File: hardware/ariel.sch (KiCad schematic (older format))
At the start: 18 parts, among them SW1 SW_Push, U1 74HC595, U2 Si7020-A20, U3 WeMos_D1_mini

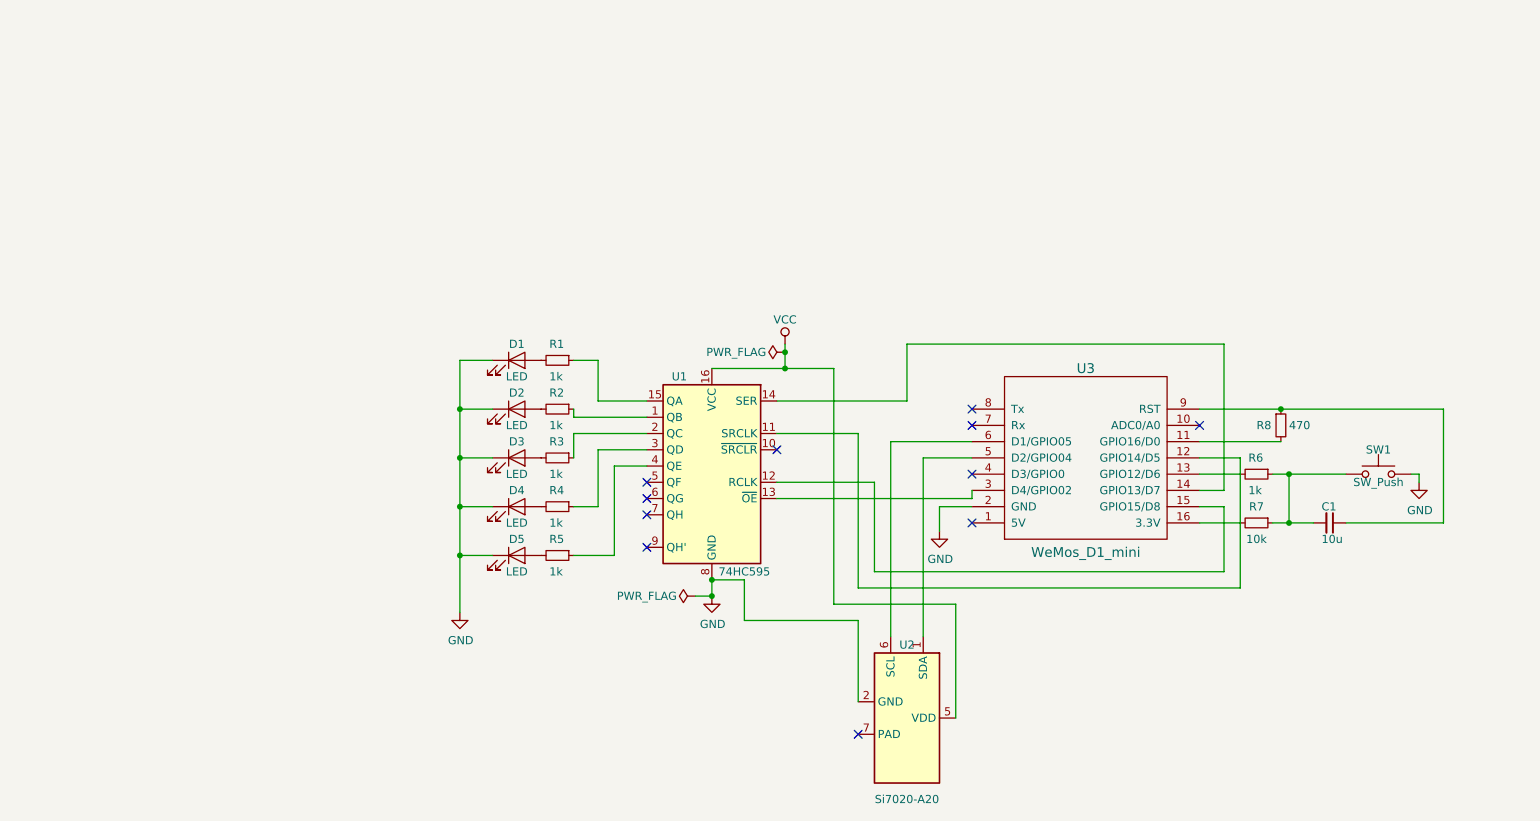
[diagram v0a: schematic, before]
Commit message: Fix power input and output
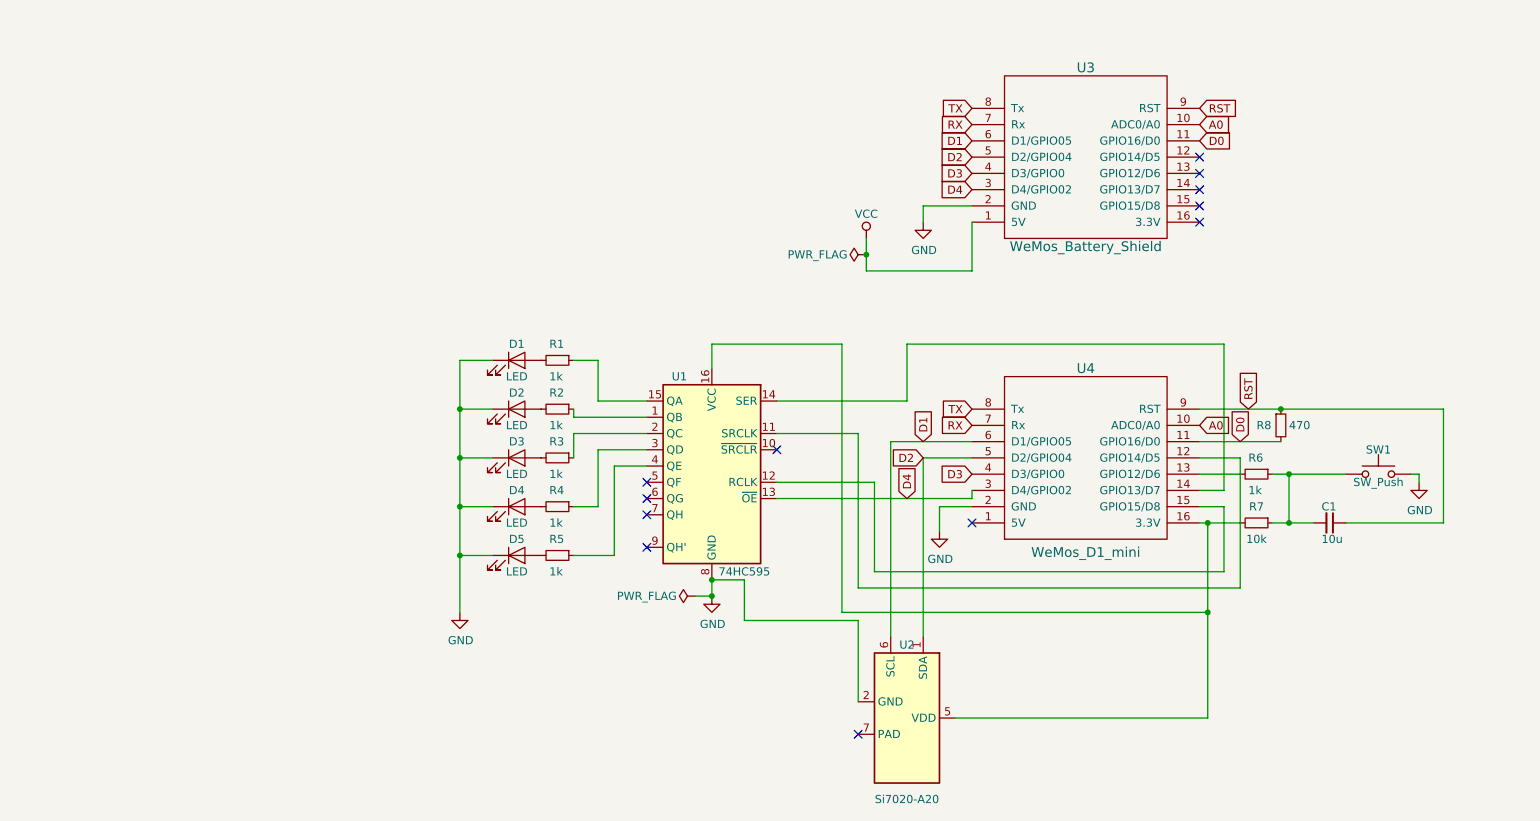
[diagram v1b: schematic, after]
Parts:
- added U3: WeMos_Battery_Shield, symbol wemos_mini:WeMos_Battery_Shield
- renumbered U3 to U4
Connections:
- net GND: now also U3.2 (GND)
- net VCC: now also U3.1 (5V); no longer U1.16 (VCC), U2.5 (VDD)
- net D4: now reaches U1.13 (~OE), U4.3 (D4/GPIO02)
- net D4: now also U3.3 (D4/GPIO02)
- net A0: now reaches U4.10 (ADC0/A0)
- net A0: now also U3.10 (ADC0/A0)
- net D0: now reaches R8.2, U4.11 (GPIO16/D0)
- net D0: now also U3.11 (GPIO16/D0)
- net at R7.2, U4.16 (3.3V): now also U1.16 (VCC), U2.5 (VDD)
- net D3: now reaches U4.4 (D3/GPIO0)
- net D3: now also U3.4 (D3/GPIO0)
- net D2: now reaches U2.1 (SDA), U4.5 (D2/GPIO04)
- net D2: now also U3.5 (D2/GPIO04)
- net D1: now reaches U2.6 (SCL), U4.6 (D1/GPIO05)
- net D1: now also U3.6 (D1/GPIO05)
- net RX: now reaches U4.7 (Rx)
- net RX: now also U3.7 (Rx)
- net TX: now reaches U4.8 (Tx)
- net TX: now also U3.8 (Tx)
- net RST: now reaches C1.1, R8.1, U4.9 (RST)
- net RST: now also U3.9 (RST)
- no-connect marks 11 -> 12
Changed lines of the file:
@@
 $EndComp
 $Comp
-L wemos_mini:WeMos_D1_mini U3
+L wemos_mini:WeMos_D1_mini U4
 U 1 1 5C77373A
 P 7500 3450
-F 0 "U3" H 7500 2900 60  0000 C CNN
+F 0 "U4" H 7500 2900 60  0000 C CNN
 F 1 "WeMos_D1_mini" H 7500 4031 60  0000 C CNN
 F 2 "" H 7900 2750 60  0000 C CNN
@@
 	8200 3350 8700 3350
 $Comp
-L power:GND #PWR04
+L power:GND #PWR06
 U 1 1 5C8607DD
 P 9550 3600
-F 0 "#PWR04" H 9550 3350 50  0001 C CNN
+F 0 "#PWR06" H 9550 3350 50  0001 C CNN
 F 1 "GND" H 9555 3427 50  0000 C CNN
 F 2 "" H 9550 3600 50  0001 C CNN
@@
 Connection ~ 8700 3150
 $Comp
-L power:GND #PWR03
+L power:GND #PWR05
 U 1 1 5C8612CC
 P 6600 3900
-F 0 "#PWR03" H 6600 3650 50  0001 C CNN
+F 0 "#PWR05" H 6600 3650 50  0001 C CNN
 F 1 "GND" H 6605 3727 50  0000 C CNN
 F 2 "" H 6600 3900 50  0001 C CNN
@@
 Wire Wire Line
 	8450 3450 8200 3450
-Wire Wire Line
-	5950 4350 5950 2900
-$Comp
-L power:PWR_FLAG #FLG01
+$Comp
+L power:PWR_FLAG #FLG02
 U 1 1 5C86A0B5
-P 5650 2800
-F 0 "#FLG01" H 5650 2875 50  0001 C CNN
-F 1 "PWR_FLAG" V 5650 3100 50  0000 C CNN
-F 2 "" H 5650 2800 50  0001 C CNN
-F 3 "~" H 5650 2800 50  0001 C CNN
-	1    5650 2800
+P 6150 2200
+F 0 "#FLG02" H 6150 2275 50  0001 C CNN
+F 1 "PWR_FLAG" V 6150 2500 50  0000 C CNN
+F 2 "" H 6150 2200 50  0001 C CNN
+F 3 "~" H 6150 2200 50  0001 C CNN
+	1    6150 2200
 	0    -1   -1   0
 $EndComp
@@
 $EndComp
 Wire Wire Line
-	5950 4350 6700 4350
-Wire Wire Line
 	6500 4550 6500 3450
 Wire Wire Line
@@
 	6300 3350 6800 3350
 NoConn ~ 6100 5150
-Wire Wire Line
-	6700 5050 6700 4350
 Wire Wire Line
 	6100 4950 6100 4450
@@
 $EndComp
 NoConn ~ 5600 3400
-NoConn ~ 6800 3150
-NoConn ~ 6800 3250
-NoConn ~ 6800 3550
-NoConn ~ 6800 3850
-NoConn ~ 8200 3250
 NoConn ~ 4800 3600
 NoConn ~ 4800 3700
@@
 Wire Wire Line
 	3650 3150 3850 3150
-Wire Wire Line
-	5650 2900 5950 2900
-Wire Wire Line
-	5650 2900 5200 2900
-Connection ~ 5650 2900
-$Comp
-L power:VCC #PWR0101
-U 1 1 5C8ADDF0
-P 5650 2750
-F 0 "#PWR0101" H 5650 2600 50  0001 C CNN
-F 1 "VCC" H 5650 2900 50  0000 C CNN
-F 2 "" H 5650 2750 50  0001 C CNN
-F 3 "" H 5650 2750 50  0001 C CNN
-	1    5650 2750
-	1    0    0    -1
-$EndComp
-Wire Wire Line
-	5650 2750 5650 2800
-Connection ~ 5650 2800
-Wire Wire Line
-	5650 2800 5650 2900
-$Comp
-L power:PWR_FLAG #FLG0101
+$Comp
+L power:PWR_FLAG #FLG01
 U 1 1 5C8B6759
 P 5100 4300
-F 0 "#FLG0101" H 5100 4375 50  0001 C CNN
+F 0 "#FLG01" H 5100 4375 50  0001 C CNN
 F 1 "PWR_FLAG" V 5100 4600 50  0000 C CNN
 F 2 "" H 5100 4300 50  0001 C CNN
@@
 	3650 4050 3650 4400
 Wire Wire Line
-	8200 3850 8450 3850
+	8200 3850 8250 3850
+$Comp
+L wemos_mini:WeMos_Battery_Shield U3
+U 1 1 5C885570
+P 7500 1600
+F 0 "U3" H 7500 1050 60  0000 C CNN
+F 1 "WeMos_Battery_Shield" H 7500 2150 60  0000 C CNN
+F 2 "" H 7900 900 60  0000 C CNN
+F 3 "http://www.wemos.cc/Products/d1_mini.html" H 7500 2181 60  0001 C CNN
+	1    7500 1600
+	1    0    0    1
+$EndComp
+Text GLabel 6800 1300 0    50   Input ~ 0
+TX
+Text GLabel 6800 3150 0    50   Input ~ 0
+TX
+Text GLabel 6800 3250 0    50   Input ~ 0
+RX
+Text GLabel 6800 1400 0    50   Input ~ 0
+RX
+Text GLabel 6500 3350 1    50   Input ~ 0
+D1
+Text GLabel 6800 1500 0    50   Input ~ 0
+D1
+Text GLabel 6800 1600 0    50   Input ~ 0
+D2
+Text GLabel 6500 3450 0    50   Input ~ 0
+D2
+Text GLabel 6800 3550 0    50   Input ~ 0
+D3
+Text GLabel 6800 1700 0    50   Input ~ 0
+D3
+Text GLabel 6400 3700 1    50   Input ~ 0
+D4
+Text GLabel 6800 1800 0    50   Input ~ 0
+D4
+$Comp
+L power:GND #PWR04
+U 1 1 5C893BFC
+P 6500 2000
+F 0 "#PWR04" H 6500 1750 50  0001 C CNN
+F 1 "GND" H 6505 1827 50  0000 C CNN
+F 2 "" H 6500 2000 50  0001 C CNN
+F 3 "" H 6500 2000 50  0001 C CNN
+	1    6500 2000
+	1    0    0    -1
+$EndComp
+Wire Wire Line
+	6800 1900 6500 1900
+Wire Wire Line
+	6500 1900 6500 2000
+Text GLabel 8200 1300 2    50   Input ~ 0
+RST
+Text GLabel 8500 3150 1    50   Input ~ 0
+RST
+Text GLabel 8200 1400 2    50   Input ~ 0
+A0
+Text GLabel 8200 3250 2    50   Input ~ 0
+A0
+Text GLabel 8200 1500 2    50   Input ~ 0
+D0
+Text GLabel 8450 3350 1    50   Input ~ 0
+D0
+NoConn ~ 8200 1600
+NoConn ~ 8200 1700
+NoConn ~ 8200 1800
+NoConn ~ 8200 1900
+NoConn ~ 8200 2000
+$Comp
+L power:VCC #PWR0101
+U 1 1 5C8A5397
+P 6150 2100
+F 0 "#PWR0101" H 6150 1950 50  0001 C CNN
+F 1 "VCC" H 6150 2250 50  0000 C CNN
+F 2 "" H 6150 2100 50  0001 C CNN
+F 3 "" H 6150 2100 50  0001 C CNN
+	1    6150 2100
+	1    0    0    -1
+$EndComp
+Wire Wire Line
+	6800 2000 6800 2300
+Wire Wire Line
+	6800 2300 6150 2300
+Wire Wire Line
+	6150 2100 6150 2200
+Connection ~ 6150 2200
+Wire Wire Line
+	6150 2200 6150 2300
+Wire Wire Line
+	5200 2750 5200 2900
+Wire Wire Line
+	8250 3850 8250 4400
+Wire Wire Line
+	8250 5050 6700 5050
+Connection ~ 8250 3850
+Wire Wire Line
+	8250 3850 8450 3850
+NoConn ~ 6800 3850
+Wire Wire Line
+	5200 2750 6000 2750
+Wire Wire Line
+	6000 2750 6000 4400
+Wire Wire Line
+	6000 4400 8250 4400
+Connection ~ 8250 4400
+Wire Wire Line
+	8250 4400 8250 5050
 $EndSCHEMATC

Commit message: Cleanup schematic and pass ERC
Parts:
- renumbered R6 to R1, R7 to R2, R8 to R3, R1 to R4, R2 to R5, R3 to R6, R4 to R7, R5 to R8, U3 to U1, U4 to U3, U1 to U4
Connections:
- net QB: now reaches R5.1, U4.1 (QB)
- net D5: now reaches U3.12 (GPIO14/D5), U4.11 (SRCLK)
- net D8: now reaches U3.15 (GPIO15/D8), U4.12 (RCLK)
- net D7: now reaches U3.14 (GPIO13/D7), U4.14 (SER)
- net QA: now reaches R4.1, U4.15 (QA)
- net 3_3V: now reaches R2.2, U2.5 (VDD), U3.16 (3.3V), U4.16 (VCC)
- net 3_3V: now also U1.16 (3.3V)
- net QC: now reaches R6.1, U4.2 (QC)
- net QD: now reaches R7.1, U4.3 (QD)
- net QE: now reaches R8.1, U4.4 (QE)
- net D6: now reaches R1.2, U3.13 (GPIO12/D6)
- no-connect marks 12 -> 11
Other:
- note added: "Battery shield is connected to a LiPo battery."
- note added: "Button circuit"
- note added: "Humidity RH% | LED ON\n0 - 20 | D1\n21 - 40 | D1, D2\n41 - 60 | D1, D2, D3\n61 - 80 | D1, D2, D3, D4\n81 - 100 | D1, D2, D3, D4, D5"
- note added: "Humidity values are displayed in the LEDs."
- note added: "LED Circuit"
- note added: "On button press, ESP8266 will wake up and \ndisplay the humidity values in the LEDs."
- note added: "Sensor circuit"
- note added: "WeMos Battery Shield"
- note added: "WeMos D1 Mini v3.0.0"
- note added: "WeMos remains in deep sleep for 6 hours and wakes \nup to sense the humidity value, display it in the LEDs \nand post the value to the cloud."
- moved on the sheet: C1, D1, D2, D3, D4, D5, R1, R2, R3, R4, R5, R6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

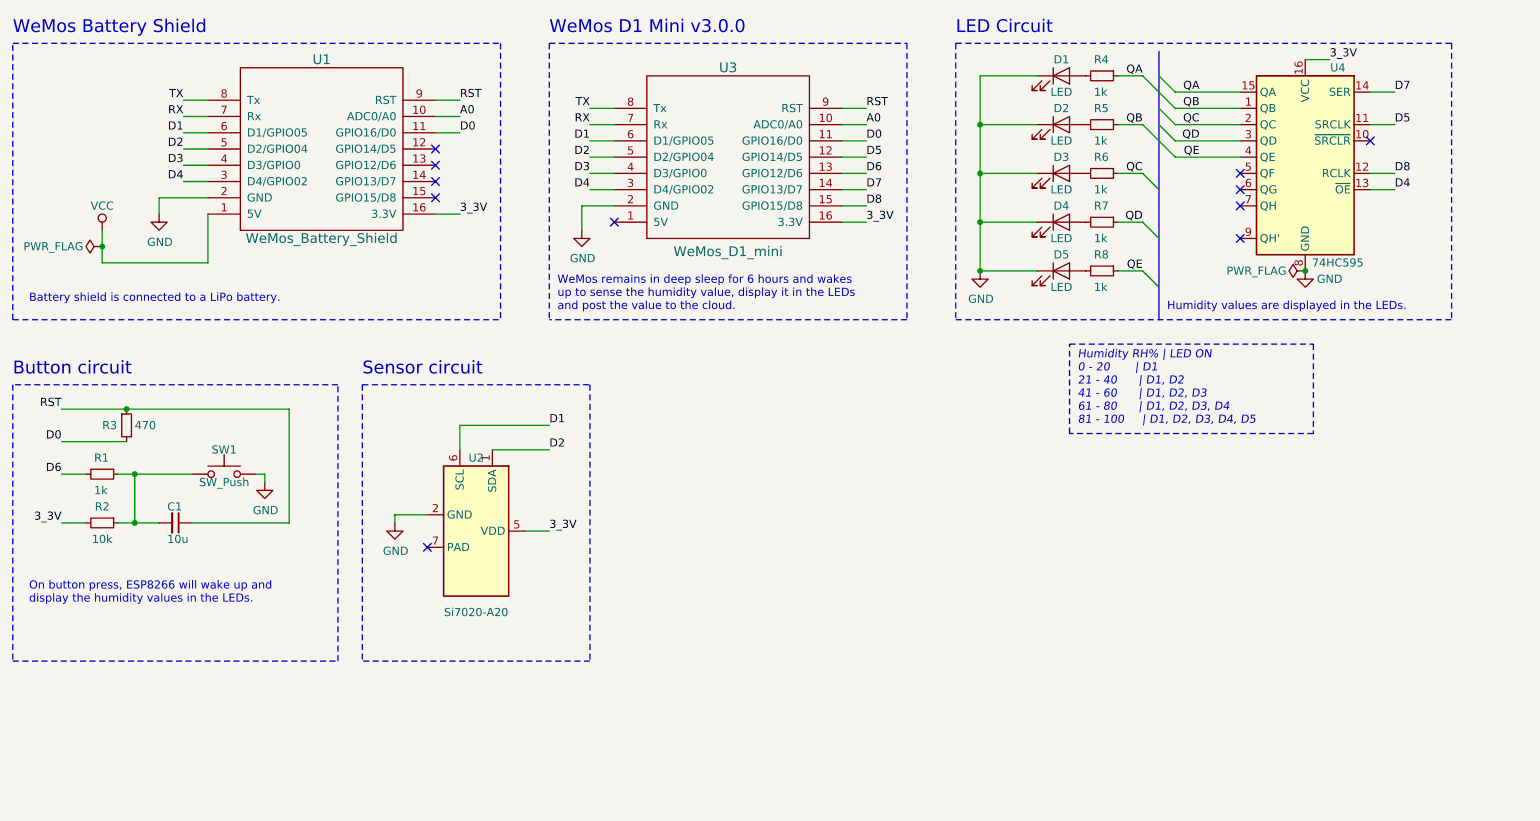
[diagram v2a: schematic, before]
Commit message: Edit labels, fix data bus
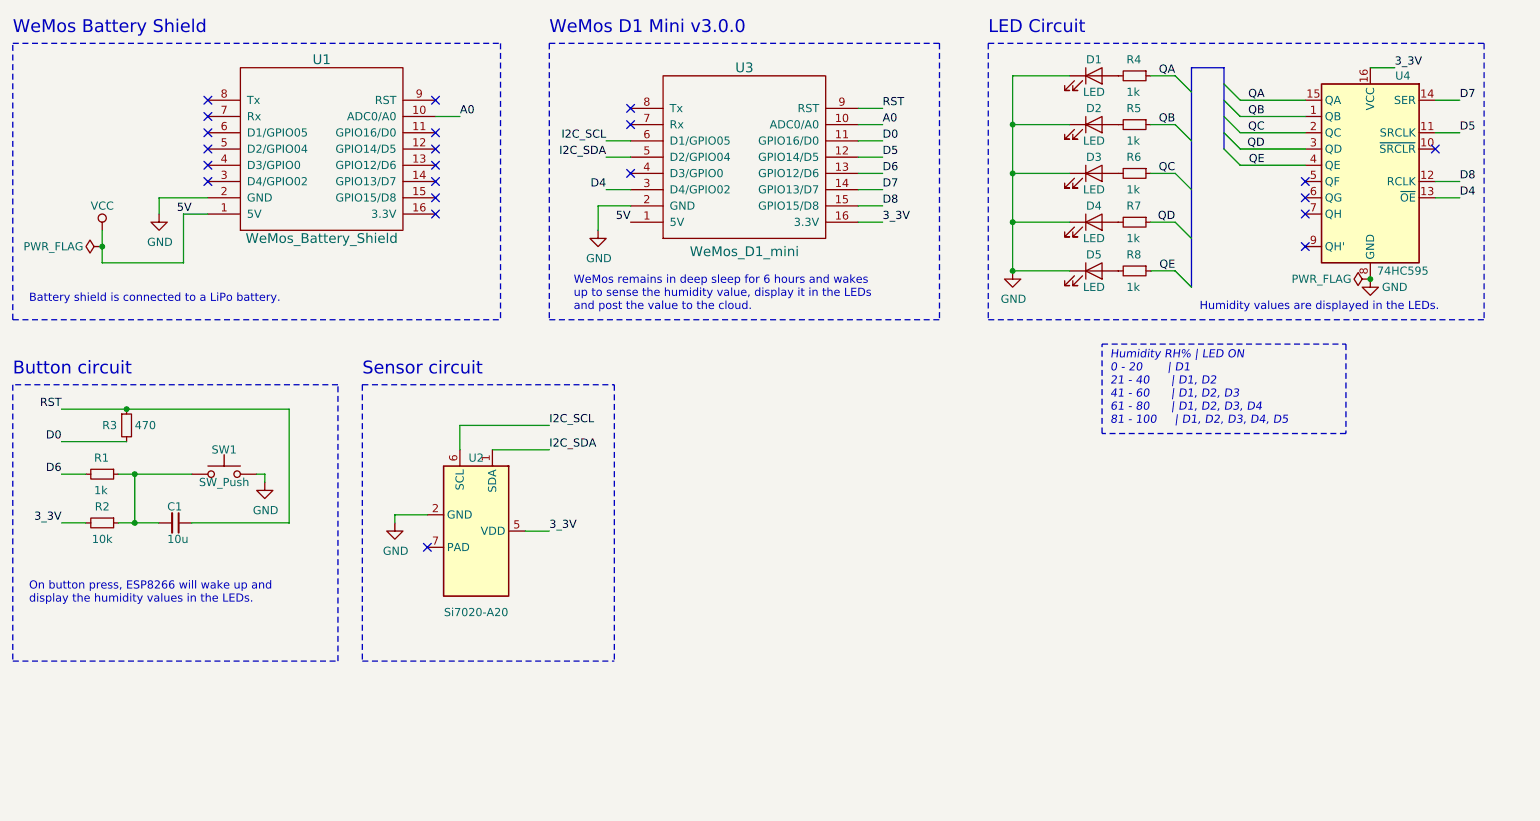
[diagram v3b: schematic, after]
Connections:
- net 3_3V: no longer U1.16 (3.3V)
- net D0: no longer U1.11 (GPIO16/D0)
- net D4: no longer U1.3 (D4/GPIO02)
- net RST: no longer U1.9 (RST)
- net VCC: now also U3.1 (5V)
- net D1 renamed I2C_SCL
- net I2C_SCL: no longer U1.6 (D1/GPIO05)
- net D2 renamed I2C_SDA
- net I2C_SDA: no longer U1.5 (D2/GPIO04)
- net D3: no longer names the net of U3.4 (D3/GPIO0)
- net D3: no longer U1.4 (D3/GPIO0)
- net RX: no longer names the net of U3.7 (Rx)
- net RX: no longer U1.7 (Rx)
- net TX: no longer names the net of U3.8 (Tx)
- net TX: no longer U1.8 (Tx)
- no-connect marks 11 -> 22
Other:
- moved on the sheet: D1, D2, D3, D4, D5, R4, R5, R6, R7, R8, U3, U4
